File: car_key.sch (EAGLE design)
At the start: 2 parts, among them U2 ATMEGA328P-AU

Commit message: Major additions
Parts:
- added C10: 1pF, resistor:C-EUC0805
- added C11: 2.2nF, resistor:C-EUC0805
- added C12: 4.7pF, resistor:C-EUC0805
- added C13: 33nF, resistor:C-EUC0805
- added C14: 10nF, resistor:C-EUC0805
- added C15: 1nF, resistor:C-EUC0805
- added C16, C17: 22pF, resistor:C-EUC0805
- added C18, C7, C8: 100uF, Wurth_Elektronik_Passive_Capacitors_rev18b:WCAP-ASLI_6,3X7,7_865080445010
- added C2, C3, C4, C5, C6: 0.1uF, rcl:C-EUC0805
- added C9: 1.5pF, resistor:C-EUC0805
- added E1: ANTENNA-GROUNDEDTRACE-25.7MM, SparkFun-RF:ANTENNA-GROUNDEDTRACE-25.7MM
- added FTDI: 61300611121, Headers:61300611121
- added I2C: 61300211121, Headers:61300211121
- added IC1: MAX3232ECD, MAX3232ECD:MAX3232ECD
- added IC2: LM1117MPX-3.3_NOPB, LM1117MPX-3.3_NOPB:LM1117MPX-3.3_NOPB
- added IC3: NRF24L01P-R7, NRF24L01P-R7:NRF24L01P-R7
- added IC4: LM1117MPX-5.0_NOPB, LM1117MPX-5.0_NOPB:LM1117MPX-5.0_NOPB
- added L1: 8.2nH, rcl:L-EUL2012C
- added L2: 2.7nH, rcl:L-EUL2012C
- added L3: 3.9nH, rcl:L-EUL2012C
- added Q1: 16M, crystal:CRYSTALHC49S
- added R1, R2, R3, R4: (no value), rcl:R-EU_R0805
- added R5, R6: 1K, rcl:R-EU_R0805
- added R7: 1M, rcl:R-EU_R0805
- added R8: 22K, rcl:R-EU_R0805
- added R9: 10K, rcl:R-EU_R0805
- added RS232: (no value), Wurth_Elektronik_Electromechanic_Input-Output_Connectors_rev19b:61800929321
- added Y1: 8MHz, SparkFun-Clocks:RESONATOR-8MHZSMD_3.2X1.3
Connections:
- new net CE: IC3.CE
- new net CSN: IC3.CSN
- new net DTR: FTDI.6
- new net FTDI_VCC: FTDI.3
- new net INT: IC3.IRQ
- new net MISO: IC3.MISO
- new net MOSI: IC3.MOSI
- new net N$10: C4.1, IC1.C2+
- new net N$11: C6.1, IC1.V+
- new net N$12: IC1.RIN1, RS232.3
- new net N$13: IC1.DOUT1, RS232.2
- new net N$14: IC3.ANT2, L1.1, L3.1
- new net N$15: IC3.ANT1, L1.2, L2.1
- new net N$16: C11.1, C12.1, IC3.VDD_PA, L2.2
- new net N$17: C9.1, L3.2
- new net N$18: C10.2, C9.2, E1.SIGNAL
- new net N$19: C13.1, IC3.DVDD
- new net N$2: R7.2, U2.(PCINT6/XTAL1/TOSC1)PB6, Y1.1
- new net N$21: C16.2, IC3.XC2, Q1.1, R9.1
- new net N$22: C17.2, IC3.XC1, Q1.2, R9.2
- new net N$23: IC3.IREF, R8.1
- new net N$3: R7.1, U2.(PCINT7/XTAL2/TOSC2)PB7, Y1.3
- new net N$4: IC1.DIN1, R5.1
- new net N$5: IC1.ROUT1, R6.1
- new net N$6: C5.1, IC1.V-
- new net N$7: C3.2, IC1.C1+
- new net N$8: C4.2, IC1.C2-
- new net N$9: C3.1, IC1.C1-
- new net RAW: C8.1, IC2.INPUT, IC4.INPUT
- new net RX-I: FTDI.4, R2.1, R4.2, R6.2, U2.PD0(RXD/PCINT16)
- new net SCK: IC3.SCK
- new net SCL: I2C.2, U2.(ADC5/SCL/PCINT13)PC5
- new net SDA: I2C.1, U2.(ADC4/SDA/PCINT12)PC4
- new net TX-O: FTDI.5, R1.1, R3.2, R5.2, U2.PD1(TXD/PCINT17)
- new net VCC/2: C18.1, IC4.OUTPUT, IC4.VOUT
- net GND: now also C10.1, C11.2, C12.2, C13.2, C14.2, C15.2, C16.1, C17.1, C18.2, C2.2, C5.2, C7.2, C8.2, E1.GND, FTDI.1, FTDI.2, IC1.GND, IC2.ADJ/GND, IC3.VSS_1, IC3.VSS_2, IC3.VSS_3, IC3.VSS_4, IC4.ADJ/GND, R1.2, R2.2, R8.2, RS232.5, Y1.2
- net VCC: now also C14.1, C15.1, C2.1, C6.2, C7.1, IC1.VCC, IC2.OUTPUT, IC2.VOUT, IC3.VDD_1, IC3.VDD_2, IC3.VDD_3, R3.1, R4.1
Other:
- note added: "TODO: Pull up/down I2C FTDI VCC Diode Relay Section Reset Section (button, FTDI) Power IO Pins Add unsused pins to header"

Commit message: progress
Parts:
- removed FTDI: 61300611121, Headers:61300611121
- removed I2C: 61300211121, Headers:61300211121
- removed R3, R4: (no value), rcl:R-EU_R0805
- removed R5, R6: 1K, rcl:R-EU_R0805
- removed RS232: (no value), Wurth_Elektronik_Electromechanic_Input-Output_Connectors_rev19b:61800929321
- added C19, C20: 0.1uF, rcl:C-EUC0805
- added D1, D2: (no value), diode:DIODE-SOD123
- added JP1: ICSP, pinhead:PINHD-2X3
- added JP2: FTDI, pinhead:PINHD-1X6
- added JP3: Digital 2, pinhead:PINHD-1X6
- added JP4: Analog, pinhead:PINHD-1X6
- added JP5: Digital 1, pinhead:PINHD-1X8
- added JP6: Power, pinhead:PINHD-1X6
- added JP7: Battery, pinhead:PINHD-2X2
- added R10, R11: 10k, rcl:R-EU_R0805
- added R12: 10K, rcl:R-EU_R0805
- added SJ1: (no value), jumper:SJ
- added X1: 2510-, con-3m:2510-
- R1, R2: value (none) -> 1K
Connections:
- removed net RAW: C8.1, IC2.INPUT, IC4.INPUT
- new net BAT: C8.1, D2.A, JP7.1, JP7.3
- new net N$20: JP4.6, U2.(ADC0/PCINT8)PC0
- new net N$24: JP4.5, U2.(ADC1/PCINT9)PC1
- new net N$25: JP4.4, U2.(ADC2/PCINT10)PC2
- new net N$26: JP4.3, U2.(ADC3/PCINT11)PC3
- new net N$27: D1.C, D2.C, IC2.INPUT, IC4.INPUT
- new net N$28: C20.2, SJ1.1
- new net N$29: JP5.4, U2.PD3(PCINT19/OC2B/INT1)
- new net N$30: JP5.5, U2.PD4(PCINT20/XCK/T0)
- new net N$31: JP5.6, U2.PD5(PCINT21/OC0B/T1)
- new net N$32: JP5.7, U2.PD6(PCINT22/OC0A/AIN0)
- new net RESET: C20.1, JP1.5, JP6.5, R12.1, U2.(RESET/PCINT14)PC6
- new net S_LOCK: JP3.6, U2.(PCINT0/CLKO/ICP1)PB0
- new net S_UNLOCK: JP5.8, U2.PD7(PCINT23/AIN1)
- net CE: now also JP3.5, U2.(PCINT1/OC1A)PB1
- net CSN: now also JP3.4, U2.(PCINT2/SS/OC1B)PB2
- net DTR: now also JP2.1, SJ1.2; no longer FTDI.6
- net FTDI_VCC: now also D1.A, JP2.4; no longer FTDI.3
- net GND: now also C19.2, JP1.6, JP2.5, JP2.6, JP6.1, JP6.2, JP7.2, JP7.4, X1-5.KL; no longer FTDI.1, FTDI.2, R1.2, R2.2, RS232.5
- net INT: now also JP5.3, U2.PD2(INT0/PCINT18)
- net MISO: now also JP1.1, JP3.2, U2.(PCINT4/MISO)PB4
- net MOSI: now also JP1.4, JP3.3, U2.(PCINT3/OC2A/MOSI)PB3
- net N$12: now also X1-3.KL; no longer RS232.3
- net N$13: now also X1-2.KL; no longer RS232.2
- net N$4: now also JP5.1, R1.1; no longer IC1.DIN1, R5.1
- net N$5: now also JP5.2, R2.1; no longer IC1.ROUT1, R6.1
- net RX-I: now also IC1.ROUT1, JP2.3, R1.2; no longer FTDI.4, R2.1, R4.2, R6.2
- net SCK: now also JP1.3, JP3.1, U2.(SCK/PCINT5)PB5
- net SCL: now also JP4.1, R10.1; no longer I2C.2
- net SDA: now also JP4.2, R11.1; no longer I2C.1
- net TX-O: now also IC1.DIN1, JP2.2, R2.2; no longer FTDI.5, R1.1, R3.2, R5.2
- net VCC: now also C19.1, JP1.2, JP6.4, JP6.6, R10.2, R11.2, R12.2; no longer R3.1, R4.1
- net VCC/2: now also JP6.3
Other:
- note added: "Auto off"
- note added: "TODO: FTDI VCC Diode Relay Section Reset Button Self kill on low power Button to kick-start"
- note removed: "TODO: Pull up/down I2C FTDI VCC Diode Relay Section Reset Section (button, FTDI) Power IO Pins Add unsused pins to header"
- moved on the sheet: C1, C2, C3, C4, C5, C6, IC1, R1, R2, R7, Y1

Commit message: changes
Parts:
- added Q2: BSS816NWH6327XTSA1, BSS816NWH6327XTSA1:BSS816NWH6327XTSA1
- added R3, R4: 10K, rcl:R-EU_R0805
- added R5: 2K, rcl:R-EU_R0805
- added SW1, SW2: B3U-1000P, Switch:B3U-1000P
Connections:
- removed net N$20: JP4.6, U2.(ADC0/PCINT8)PC0
- removed net N$32: JP5.7, U2.PD6(PCINT22/OC0A/AIN0)
- new net N$33: D2.A, Q2.S, SW1.2
- new net S_POWER: JP5.7, Q2.G, R3.2, U2.PD6(PCINT22/OC0A/AIN0)
- new net V_SENSE: JP4.6, R4.1, R5.2, U2.(ADC0/PCINT8)PC0
- net BAT: now also Q2.D, R4.2, SW1.1; no longer D2.A
- net GND: now also R3.1, R5.1, SW2.1
- net RESET: now also SW2.2
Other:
- note added: "TODO: Relay Section"
- note removed: "Auto off"
- note removed: "TODO: FTDI VCC Diode Relay Section Reset Button Self kill on low power Button to kick-start"

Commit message: changes
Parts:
- removed IC4: LM1117MPX-5.0_NOPB, LM1117MPX-5.0_NOPB:LM1117MPX-5.0_NOPB
- removed JP2: FTDI, pinhead:PINHD-1X6
- removed JP3: Digital 2, pinhead:PINHD-1X6
- removed JP4: Analog, pinhead:PINHD-1X6
- removed JP5: Digital 1, pinhead:PINHD-1X8
- removed JP6: Power, pinhead:PINHD-1X6
- removed JP7: Battery, pinhead:PINHD-2X2
- added FTDI: TSW-106-08-G-S, con-samtec:TSW-106-08-G-S
- added I2C: TSW-102-08-G-S, con-samtec:TSW-102-08-G-S
- added JP8: nRF24L01+ Module, pinhead:PINHD-2X4
- X1: value 2510- -> RS232
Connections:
- removed net N$24: JP4.5, U2.(ADC1/PCINT9)PC1
- removed net N$25: JP4.4, U2.(ADC2/PCINT10)PC2
- removed net N$26: JP4.3, U2.(ADC3/PCINT11)PC3
- removed net N$29: JP5.4, U2.PD3(PCINT19/OC2B/INT1)
- removed net N$30: JP5.5, U2.PD4(PCINT20/XCK/T0)
- removed net N$31: JP5.6, U2.PD5(PCINT21/OC0B/T1)
- net BAT: no longer JP7.1, JP7.3
- net CE: now also JP8.3; no longer JP3.5
- net CSN: now also JP8.4; no longer JP3.4
- net DTR: now also FTDI-1.1; no longer JP2.1
- net FTDI_VCC: now also FTDI-4.1; no longer JP2.4
- net GND: now also FTDI-5.1, FTDI-6.1, JP8.1; no longer IC4.ADJ/GND, JP2.5, JP2.6, JP6.1, JP6.2, JP7.2, JP7.4
- net INT: now also JP8.8; no longer JP5.3
- net MISO: now also JP8.7; no longer JP3.2
- net MOSI: now also JP8.6; no longer JP3.3
- net N$27: no longer IC4.INPUT
- net N$4: now also U2.PD1(TXD/PCINT17); no longer JP5.1
- net N$5: now also U2.PD0(RXD/PCINT16); no longer JP5.2
- net RESET: no longer JP6.5
- net RX-I: now also FTDI-3.1, R2.2; no longer JP2.3, R1.2, U2.PD0(RXD/PCINT16)
- net SCK: now also JP8.5; no longer JP3.1
- net SCL: now also I2C-1.1; no longer JP4.1
- net SDA: now also I2C-2.1; no longer JP4.2
- net S_LOCK: no longer JP3.6
- net S_POWER: no longer JP5.7
- net S_UNLOCK: no longer JP5.8
- net TX-O: now also FTDI-2.1, R1.2; no longer JP2.2, R2.2, U2.PD1(TXD/PCINT17)
- net VCC: now also JP8.2; no longer JP6.4, JP6.6
- net VCC/2: no longer IC4.OUTPUT, IC4.VOUT, JP6.3
- net V_SENSE: no longer JP4.6
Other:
- note added: "TODO: Relay Section (relays, leds, mosfets)"
- note removed: "TODO: Relay Section"
- moved on the sheet: R1, R2

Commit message: changes
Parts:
- removed C8: 100uF, Wurth_Elektronik_Passive_Capacitors_rev18b:WCAP-ASLI_6,3X7,7_865080445010
- removed IC2: LM1117MPX-3.3_NOPB, LM1117MPX-3.3_NOPB:LM1117MPX-3.3_NOPB
- removed Q2: BSS816NWH6327XTSA1, BSS816NWH6327XTSA1:BSS816NWH6327XTSA1
- added C21: 10u, Wurth_Elektronik_Passive_Capacitors_rev18b:WCAP-ASLI_4X5,5_865080340001
- added IC4: TPS562231DRLR, TPS562231DRLR:TPS562231DRLR
- added L4: DFE322520FD-3R3M=P2, DFE322520FD-3R3M=P2:DFE322520FD-3R3M=P2
- added Q3: FDN360P, transistor-power:FDN360P
- added R13: 2.2k, rcl:R-EU_R0805
- added R14: 100, rcl:R-EU_R0805
- added R15: 10k, rcl:R-EU_R0805
- added R6: 43k, rcl:R-EU_R0805
- C18: value 100uF -> 0.1u; device Wurth_Elektronik_Passive_Capacitors_rev18b:WCAP-ASLI_6,3X7,7_865080445010 -> rcl:C-EUC0805
- C7: value 100uF -> 47u; device Wurth_Elektronik_Passive_Capacitors_rev18b:WCAP-ASLI_6,3X7,7_865080445010 -> Wurth_Elektronik_Passive_Capacitors_rev18b:WCAP-ASLI_4X5,5_865080140004
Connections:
- removed net VCC/2: C18.1
- new net N$24: C18.1, IC4.SW, L4.1
- new net N$25: C18.2, IC4.BST
- new net N$26: R13.2, R14.2
- new net N$30: R13.1, R6.1
- new net N$31: IC4.FB, R14.1, R15.2
- net BAT: now also Q3.S; no longer C8.1, Q2.D
- net GND: now also C21.2, IC4.GND, R15.1; no longer C18.2, C8.2, IC2.ADJ/GND
- net N$27: now also C21.1, IC4.EN, IC4.VIN; no longer IC2.INPUT
- net N$33: now also Q3.D; no longer Q2.S
- net S_POWER: now also Q3.G; no longer Q2.G
- net VCC: now also L4.2, R6.2; no longer IC2.OUTPUT, IC2.VOUT
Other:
- moved on the sheet: C7, FTDI-1, FTDI-2, FTDI-3, FTDI-4, FTDI-5, FTDI-6, R3, SW1

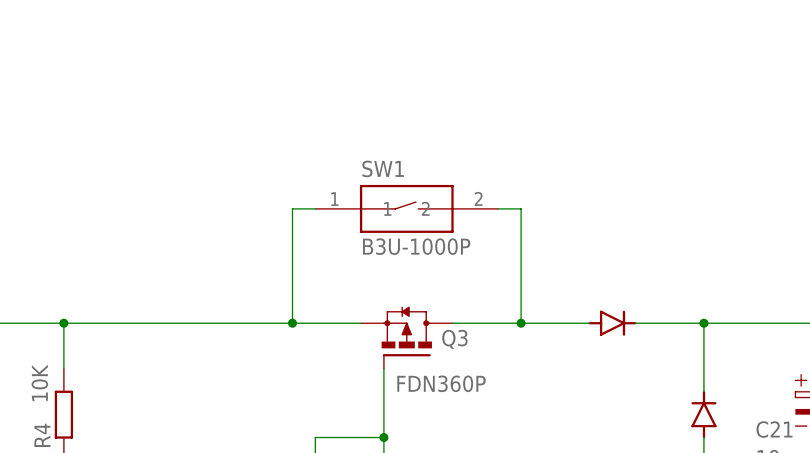
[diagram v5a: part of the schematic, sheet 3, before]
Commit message: move psu, labels
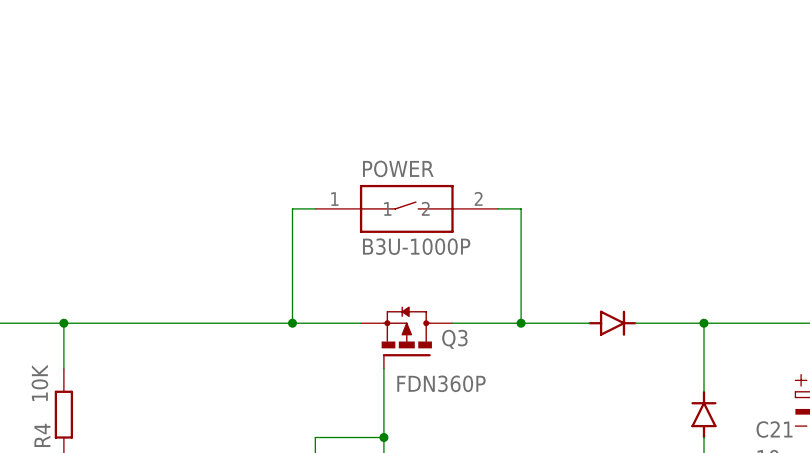
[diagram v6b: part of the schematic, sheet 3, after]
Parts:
- renumbered SW1 to POWER
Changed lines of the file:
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@@
 <?xml version="1.0" encoding="utf-8"?>
 <!DOCTYPE eagle SYSTEM "eagle.dtd">
-<eagle version="9.5.0">
+<eagle version="9.5.1">
 <drawing>
 <settings>
@@
 <part name="R4" library="rcl" library_urn="urn:adsk.eagle:library:334" deviceset="R-EU_" device="R0805" package3d_urn="urn:adsk.eagle:package:23553/2" value="10K"/>
 <part name="R5" library="rcl" library_urn="urn:adsk.eagle:library:334" deviceset="R-EU_" device="R0805" package3d_urn="urn:adsk.eagle:package:23553/2" value="2K"/>
-<part name="SW1" library="Switch" library_urn="urn:adsk.eagle:library:11396471" deviceset="B3U-1000P" device="" package3d_urn="urn:adsk.eagle:package:10899220/2"/>
+<part name="POWER" library="Switch" library_urn="urn:adsk.eagle:library:11396471" deviceset="B3U-1000P" device="" package3d_urn="urn:adsk.eagle:package:10899220/2"/>
 <part name="SW2" library="Switch" library_urn="urn:adsk.eagle:library:11396471" deviceset="B3U-1000P" device="" package3d_urn="urn:adsk.eagle:package:10899220/2"/>
 <part name="GND27" library="supply1" library_urn="urn:adsk.eagle:library:371" deviceset="GND" device=""/>
@@
 <attribute name="VALUE" x="36.322" y="80.01" size="1.778" layer="96" rot="R90"/>
 </instance>
-<instance part="SW1" gate="G$1" x="76.2" y="116.84" smashed="yes">
+<instance part="POWER" gate="G$1" x="76.2" y="116.84" smashed="yes">
 <attribute name="NAME" x="71.12" y="120.396" size="1.778" layer="95"/>
 <attribute name="VALUE" x="71.12" y="111.76" size="1.778" layer="96"/>
@@
 <wire x1="63.5" y1="116.84" x2="66.04" y2="116.84" width="0.1524" layer="91"/>
 <junction x="63.5" y="104.14"/>
-<pinref part="SW1" gate="G$1" pin="1"/>
+<pinref part="POWER" gate="G$1" pin="1"/>
 <pinref part="Q3" gate="G$1" pin="S"/>
 </segment>
@@
 <junction x="88.9" y="104.14"/>
 <wire x1="88.9" y1="116.84" x2="86.36" y2="116.84" width="0.1524" layer="91"/>
-<pinref part="SW1" gate="G$1" pin="2"/>
+<pinref part="POWER" gate="G$1" pin="2"/>
 <pinref part="Q3" gate="G$1" pin="D"/>
 </segment>

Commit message: aa
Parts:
- JP8: value nRF24L01+ Module -> nRF24L01+
- renumbered SW2 to RESET
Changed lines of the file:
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@@
 <part name="R5" library="rcl" library_urn="urn:adsk.eagle:library:334" deviceset="R-EU_" device="R0805" package3d_urn="urn:adsk.eagle:package:23553/2" value="2K"/>
 <part name="POWER" library="Switch" library_urn="urn:adsk.eagle:library:11396471" deviceset="B3U-1000P" device="" package3d_urn="urn:adsk.eagle:package:10899220/2"/>
-<part name="SW2" library="Switch" library_urn="urn:adsk.eagle:library:11396471" deviceset="B3U-1000P" device="" package3d_urn="urn:adsk.eagle:package:10899220/2"/>
+<part name="RESET" library="Switch" library_urn="urn:adsk.eagle:library:11396471" deviceset="B3U-1000P" device="" package3d_urn="urn:adsk.eagle:package:10899220/2"/>
 <part name="GND27" library="supply1" library_urn="urn:adsk.eagle:library:371" deviceset="GND" device=""/>
-<part name="JP8" library="pinhead" library_urn="urn:adsk.eagle:library:325" deviceset="PINHD-2X4" device="" package3d_urn="urn:adsk.eagle:package:22461/2" value="nRF24L01+ Module"/>
+<part name="JP8" library="pinhead" library_urn="urn:adsk.eagle:library:325" deviceset="PINHD-2X4" device="" package3d_urn="urn:adsk.eagle:package:22461/2" value="nRF24L01+"/>
 <part name="GND28" library="supply1" library_urn="urn:adsk.eagle:library:371" deviceset="GND" device=""/>
 <part name="P+20" library="supply1" library_urn="urn:adsk.eagle:library:371" deviceset="VCC" device=""/>
@@
 <attribute name="VALUE" x="35.56" y="5.08" size="1.778" layer="96"/>
 </instance>
-<instance part="SW2" gate="G$1" x="190.5" y="137.16" smashed="yes">
+<instance part="RESET" gate="G$1" x="190.5" y="137.16" smashed="yes">
 <attribute name="NAME" x="185.42" y="140.716" size="1.778" layer="95"/>
 <attribute name="VALUE" x="185.42" y="132.08" size="1.778" layer="96"/>
@@
 </segment>
 <segment>
-<pinref part="SW2" gate="G$1" pin="1"/>
+<pinref part="RESET" gate="G$1" pin="1"/>
 <wire x1="180.34" y1="137.16" x2="172.72" y2="137.16" width="0.1524" layer="91"/>
 <pinref part="GND27" gate="1" pin="GND"/>
@@
 <wire x1="208.28" y1="111.76" x2="208.28" y2="137.16" width="0.1524" layer="91"/>
 <junction x="208.28" y="137.16"/>
-<pinref part="SW2" gate="G$1" pin="2"/>
+<pinref part="RESET" gate="G$1" pin="2"/>
 <wire x1="200.66" y1="137.16" x2="208.28" y2="137.16" width="0.1524" layer="91"/>
 </segment>
